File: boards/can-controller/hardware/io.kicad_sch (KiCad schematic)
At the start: 17 parts, among them J40 GPIO

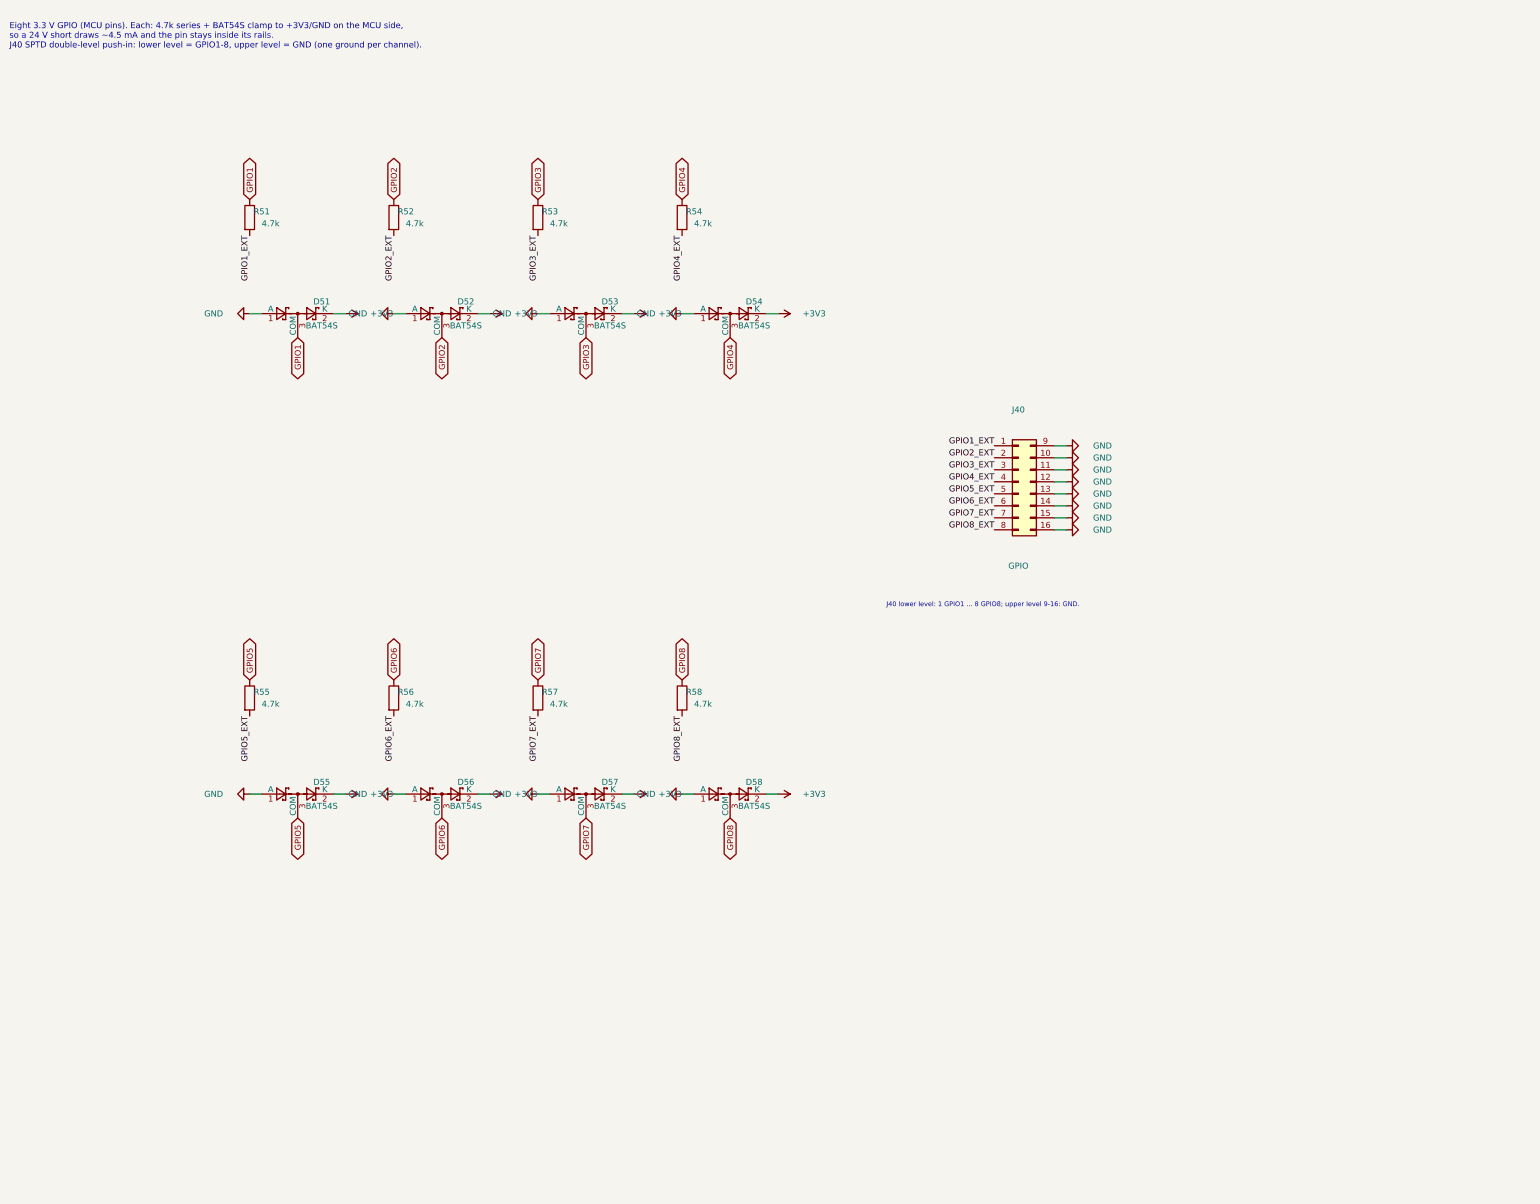
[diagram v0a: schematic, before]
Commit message: can-controller: schematic for the new scope (Ethernet W6100, 4 x ISOW1044, AQW212 relays, diff AI)
Six sheets generated by gen_schematic.py: MCU and logic power, Ethernet,
CAN x4, 12 V input and isolated logic supply (TDN 5-2411WI), relay drive,
GPIO and analog in. ERC 0; netlist check: no net crosses a domain except
at the designed crossings. New lib parts: Thl_Interface:W6100-L (flat),
Thl_Isolator:AQW212, stock ISOW1044 / TDN 5WI / LQFP-48 / bead footprints.
PCB still holds the old layout (next: update from schematic, placement).

Co-Authored-By: Claude Opus 5.5 <noreply@anthropic.com>
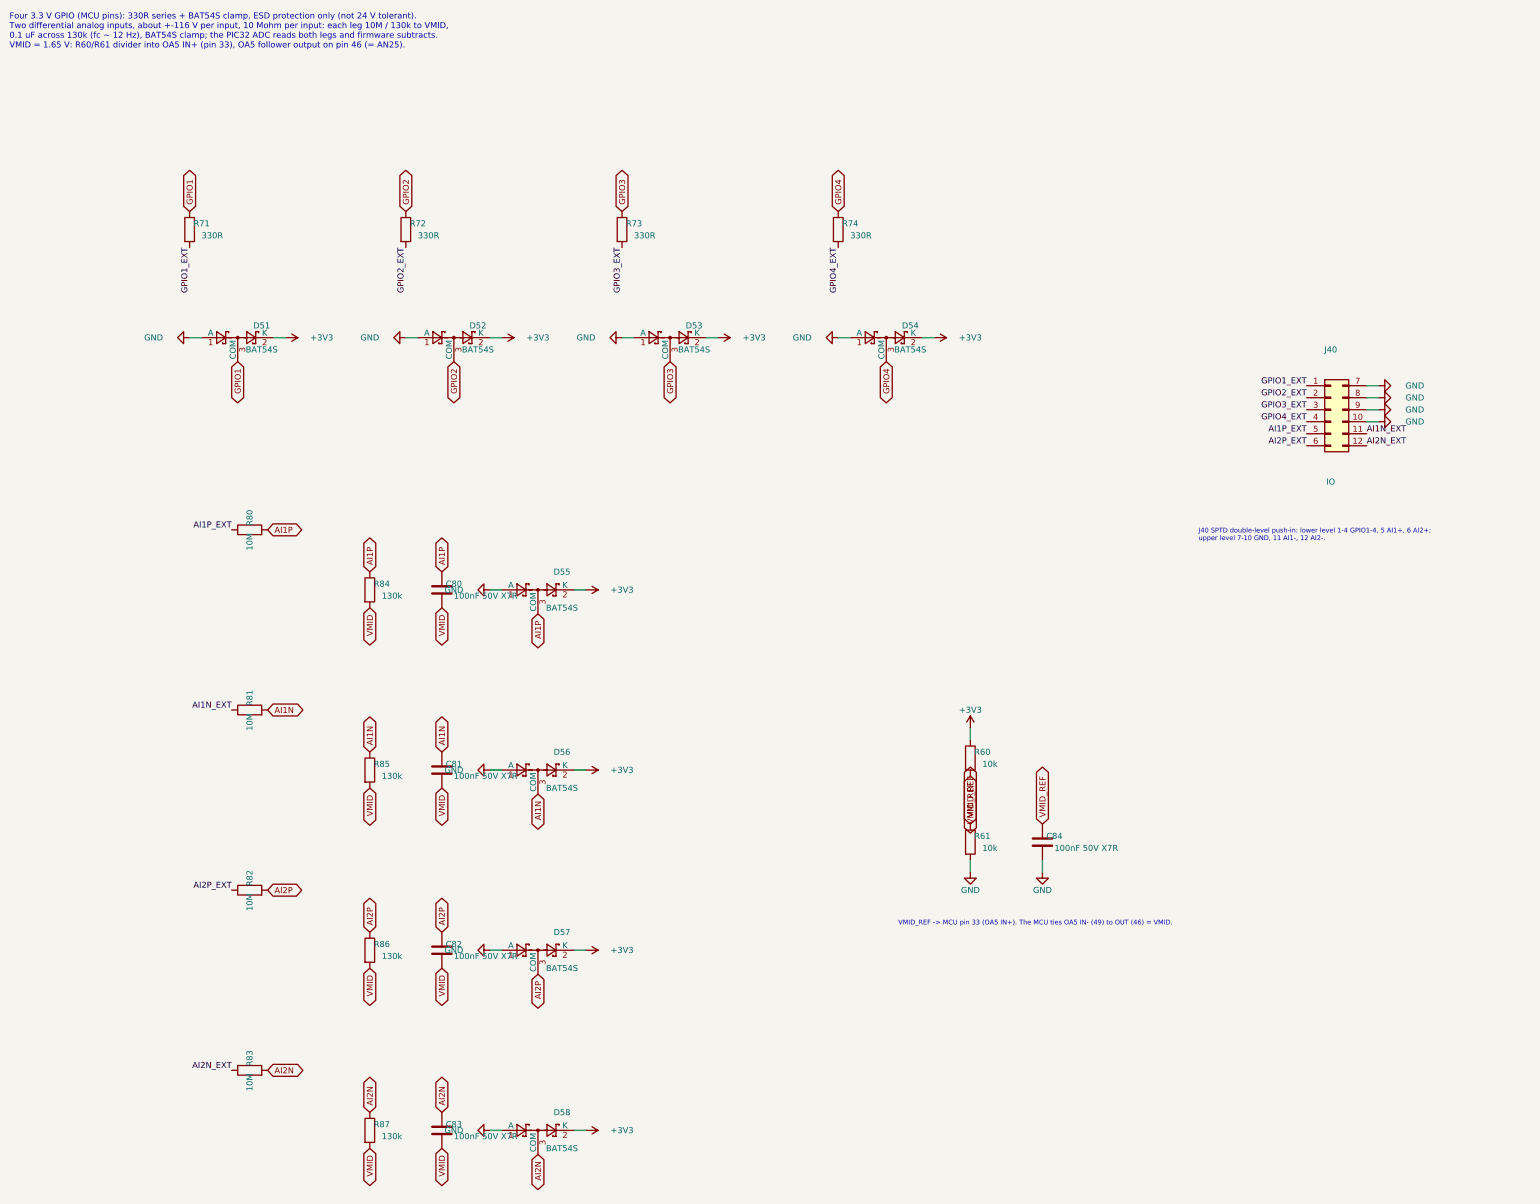
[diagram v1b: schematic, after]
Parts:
- removed J40: GPIO, Thl_Connector:PhoenixContact_SPTD_1,5_8-H-3,5_2x08_P3.5mm_Horizontal, symbol Connector_Generic:Conn_02x08_Top_Bottom
- removed R51, R52, R53, R54, R55, R56, R57, R58: 4.7k, Resistor_SMD:R_1206_3216Metric_Pad1.30x1.75mm_HandSolder, symbol Device:R
- added C80, C81, C82, C83: 100nF 50V X7R, Capacitor_SMD:C_1206_3216Metric_Pad1.33x1.80mm_HandSolder, symbol Device:C
- added C84: 100nF 50V X7R, Capacitor_SMD:C_0805_2012Metric_Pad1.18x1.45mm_HandSolder, symbol Device:C
- added J40: IO, Thl_Connector:PhoenixContact_SPTD_1,5_6-H-3,5_2x06_P3.5mm_Horizontal, symbol Connector_Generic:Conn_02x06_Top_Bottom
- added R60, R61: 10k, Resistor_SMD:R_1206_3216Metric_Pad1.30x1.75mm_HandSolder, symbol Device:R
- added R71, R72, R73, R74: 330R, Resistor_SMD:R_1206_3216Metric_Pad1.30x1.75mm_HandSolder, symbol Device:R
- added R80, R81, R82, R83: 10M, Resistor_SMD:R_1206_3216Metric_Pad1.30x1.75mm_HandSolder, symbol Device:R
- added R84, R85, R86, R87: 130k, Resistor_SMD:R_1206_3216Metric_Pad1.30x1.75mm_HandSolder, symbol Device:R
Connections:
- net +3V3: now also R60.1
- net GND: now also C84.2, J40.10 (Pin_10), J40.7 (Pin_7), J40.8 (Pin_8), J40.9 (Pin_9), R61.2
- net GPIO1: now also R71.1
- net GPIO1_EXT: now also J40.1 (Pin_1), R71.2
- net GPIO2: now also R72.1
- net GPIO2_EXT: now also J40.2 (Pin_2), R72.2
- net GPIO3: now also R73.1
- net GPIO3_EXT: now also J40.3 (Pin_3), R73.2
- net GPIO4: now also R74.1
- net GPIO4_EXT: now also J40.4 (Pin_4), R74.2
- net GPIO5 renamed AI1P
- net AI1P: now also C80.1, R80.2, R84.1
- net GPIO6 renamed AI1N
- net AI1N: now also C81.1, R81.2, R85.1
- net GPIO7 renamed AI2P
- net AI2P: now also C82.1, R82.2, R86.1
- net GPIO8 renamed AI2N
- net AI2N: now also C83.1, R83.2, R87.1
- new net AI1N_EXT: J40.11 (Pin_11), R81.1
- new net AI1P_EXT: J40.5 (Pin_5), R80.1
- new net AI2N_EXT: J40.12 (Pin_12), R83.1
- new net AI2P_EXT: J40.6 (Pin_6), R82.1
- new net VMID: C80.2, C81.2, C82.2, C83.2, R84.2, R85.2, R86.2, R87.2
- new net VMID_REF: C84.1, R60.2, R61.1
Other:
- note added: "Four 3.3 V GPIO (MCU pins): 330R series + BAT54S clamp, ESD protection only (not 24 V tolerant). Two differential analog inputs, about +-116 V per input, 10 Mohm per input: each leg 10M / 130k to VMID, 0.1 uF across 130k (fc ~ 12 Hz), BAT54S clamp; the PIC32 ADC reads both legs and firmware subtracts. VMID = 1.65 V: R60/R61 divider into OA5 IN+ (pin 33), OA5 follower output on pin 46 (= AN25)."
- note added: "J40 SPTD double-level push-in: lower level 1-4 GPIO1-4, 5 AI1+, 6 AI2+; upper level 7-10 GND, 11 AI1-, 12 AI2-."
- note added: "VMID_REF -> MCU pin 33 (OA5 IN+). The MCU ties OA5 IN- (49) to OUT (46) = VMID."
- note removed: "Eight 3.3 V GPIO (MCU pins). Each: 4.7k series + BAT54S clamp to +3V3/GND on the MCU side, so a 24 V short draws ~4.5 mA and the pin stays inside its rails. J40 SPTD double-level push-in: lower level = GPIO1-8, upper level = GND (one ground per channel)."
- note removed: "J40 lower level: 1 GPIO1 ... 8 GPIO8; upper level 9-16: GND."
- title: CAN controller: GPIO -> CAN controller: GPIO and differential analog inputs

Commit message: Move core, can-card, io-card, serial-card, can-ssr, probe-helper to rev B
Rev A went to PCBWay and is tagged revA. Rev B replaces parts the Mouser
BOM check flagged (obsolete, end of life, not recommended for new designs,
or not orderable) and swaps out-of-stock passives and diodes for in-stock
equivalents. Field-only changes, same footprints, no layout change; the
reference boards (can-controller, pic-module) get the same part numbers.
The rev A order lists (DigiKey, Mouser) carry the same substitutions; the
Mouser list leaves out the T821 box headers (bought from DigiKey).

docs/rev-b-changes.md lists every change and the rev B to-dos (MAX7219 is
obsolete and must be replaced). transfer/mouser-revA.xlsx (Mouser BOM
check) consumed.

Co-Authored-By: Claude Opus 5.5 <noreply@anthropic.com>
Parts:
- C80, C81, C82, C83: MPN GRM319R71H104KA01D -> C1206C104K5RACTU; Manufacturer Murata -> KEMET
- C84: MPN GRM21BR71H104KA01L -> C0805C104K5RACTU; Manufacturer Murata -> KEMET
- D51, D52, D53, D54, D55, D56, D57, D58: MPN BAT54S,215 -> BAT54S-7-F; Manufacturer Nexperia -> Diodes Incorporated
- R71, R72, R73, R74: MPN RC1206FR-07330RL -> RMCF1206FT330R; Manufacturer Yageo -> Stackpole
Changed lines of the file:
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@@
 			)
 		)
-		(property "Manufacturer" "Yageo"
+		(property "Manufacturer" "Stackpole"
 			(at 63.5 63.5 0)
 			(hide yes)
@@
 			)
 		)
-		(property "MPN" "RC1206FR-07330RL"
+		(property "MPN" "RMCF1206FT330R"
 			(at 63.5 63.5 0)
 			(hide yes)
@@
 			)
 		)
-		(property "Manufacturer" "Nexperia"
+		(property "Manufacturer" "Diodes Incorporated"
 			(at 73.66 86.36 0)
 			(hide yes)
@@
 			)
 		)
-		(property "MPN" "BAT54S,215"
+		(property "MPN" "BAT54S-7-F"
 			(at 73.66 86.36 0)
 			(hide yes)
@@
 			)
 		)
-		(property "Manufacturer" "Yageo"
+		(property "Manufacturer" "Stackpole"
 			(at 109.22 63.5 0)
 			(hide yes)
@@
 			)
 		)
-		(property "MPN" "RC1206FR-07330RL"
+		(property "MPN" "RMCF1206FT330R"
 			(at 109.22 63.5 0)
 			(hide yes)
@@
 			)
 		)
-		(property "Manufacturer" "Nexperia"
+		(property "Manufacturer" "Diodes Incorporated"
 			(at 119.38 86.36 0)
 			(hide yes)
@@
 			)
 		)
-		(property "MPN" "BAT54S,215"
+		(property "MPN" "BAT54S-7-F"
 			(at 119.38 86.36 0)
 			(hide yes)
@@
 			)
 		)
-		(property "Manufacturer" "Yageo"
+		(property "Manufacturer" "Stackpole"
 			(at 154.94 63.5 0)
 			(hide yes)
@@
 			)
 		)
-		(property "MPN" "RC1206FR-07330RL"
+		(property "MPN" "RMCF1206FT330R"
 			(at 154.94 63.5 0)
 			(hide yes)
@@
 			)
 		)
-		(property "Manufacturer" "Nexperia"
+		(property "Manufacturer" "Diodes Incorporated"
 			(at 165.1 86.36 0)
 			(hide yes)
@@
 			)
 		)
-		(property "MPN" "BAT54S,215"
+		(property "MPN" "BAT54S-7-F"
 			(at 165.1 86.36 0)
 			(hide yes)
@@
 			)
 		)
-		(property "Manufacturer" "Yageo"
+		(property "Manufacturer" "Stackpole"
 			(at 200.66 63.5 0)
 			(hide yes)
@@
 			)
 		)
-		(property "MPN" "RC1206FR-07330RL"
+		(property "MPN" "RMCF1206FT330R"
 			(at 200.66 63.5 0)
 			(hide yes)
@@
 			)
 		)
-		(property "Manufacturer" "Nexperia"
+		(property "Manufacturer" "Diodes Incorporated"
 			(at 210.82 86.36 0)
 			(hide yes)
@@
 			)
 		)
-		(property "MPN" "BAT54S,215"
+		(property "MPN" "BAT54S-7-F"
 			(at 210.82 86.36 0)
 			(hide yes)
@@
 			)
 		)
-		(property "Manufacturer" "Murata"
+		(property "Manufacturer" "KEMET"
 			(at 116.84 139.7 0)
 			(hide yes)
@@
 			)
 		)
-		(property "MPN" "GRM319R71H104KA01D"
+		(property "MPN" "C1206C104K5RACTU"
 			(at 116.84 139.7 0)
 			(hide yes)
@@
 			)
 		)
-		(property "Manufacturer" "Nexperia"
+		(property "Manufacturer" "Diodes Incorporated"
 			(at 137.16 139.7 0)
 			(hide yes)
@@
 			)
 		)
-		(property "MPN" "BAT54S,215"
+		(property "MPN" "BAT54S-7-F"
 			(at 137.16 139.7 0)
 			(hide yes)
@@
 			)
 		)
-		(property "Manufacturer" "Murata"
+		(property "Manufacturer" "KEMET"
 			(at 116.84 177.8 0)
 			(hide yes)
@@
 			)
 		)
-		(property "MPN" "GRM319R71H104KA01D"
+		(property "MPN" "C1206C104K5RACTU"
 			(at 116.84 177.8 0)
 			(hide yes)
@@
 			)
 		)
-		(property "Manufacturer" "Nexperia"
+		(property "Manufacturer" "Diodes Incorporated"
 			(at 137.16 177.8 0)
 			(hide yes)
@@
 			)
 		)
-		(property "MPN" "BAT54S,215"
+		(property "MPN" "BAT54S-7-F"
 			(at 137.16 177.8 0)
 			(hide yes)
@@
 			)
 		)
-		(property "Manufacturer" "Murata"
+		(property "Manufacturer" "KEMET"
 			(at 116.84 215.9 0)
 			(hide yes)
@@
 			)
 		)
-		(property "MPN" "GRM319R71H104KA01D"
+		(property "MPN" "C1206C104K5RACTU"
 			(at 116.84 215.9 0)
 			(hide yes)
@@
 			)
 		)
-		(property "Manufacturer" "Nexperia"
+		(property "Manufacturer" "Diodes Incorporated"
 			(at 137.16 215.9 0)
 			(hide yes)
@@
 			)
 		)
-		(property "MPN" "BAT54S,215"
+		(property "MPN" "BAT54S-7-F"
 			(at 137.16 215.9 0)
 			(hide yes)
@@
 			)
 		)
-		(property "Manufacturer" "Murata"
+		(property "Manufacturer" "KEMET"
 			(at 116.84 254 0)
 			(hide yes)
@@
 			)
 		)
-		(property "MPN" "GRM319R71H104KA01D"
+		(property "MPN" "C1206C104K5RACTU"
 			(at 116.84 254 0)
 			(hide yes)
@@
 			)
 		)
-		(property "Manufacturer" "Nexperia"
+		(property "Manufacturer" "Diodes Incorporated"
 			(at 137.16 254 0)
 			(hide yes)
@@
 			)
 		)
-		(property "MPN" "BAT54S,215"
+		(property "MPN" "BAT54S-7-F"
 			(at 137.16 254 0)
 			(hide yes)
@@
 			)
 		)
-		(property "Manufacturer" "Murata"
+		(property "Manufacturer" "KEMET"
 			(at 243.84 193.04 0)
 			(hide yes)
@@
 			)
 		)
-		(property "MPN" "GRM21BR71H104KA01L"
+		(property "MPN" "C0805C104K5RACTU"
 			(at 243.84 193.04 0)
 			(hide yes)
